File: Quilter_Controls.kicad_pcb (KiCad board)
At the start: 2 copper layers, 40.4 x 110 mm, 19 parts, among them J1 Conn_01x10_Male, J10 Conn_01x04_Male, J11 Freq_In, J2 Conn_01x10_Male, J3 Conn_01x10_Male, J4 Audio_In, J5 Audio_Out, J6 Audio_Mix, J7 Freq_V_Oct, J8 Freq_CV, J9 Conn_02x04_Top_Bottom

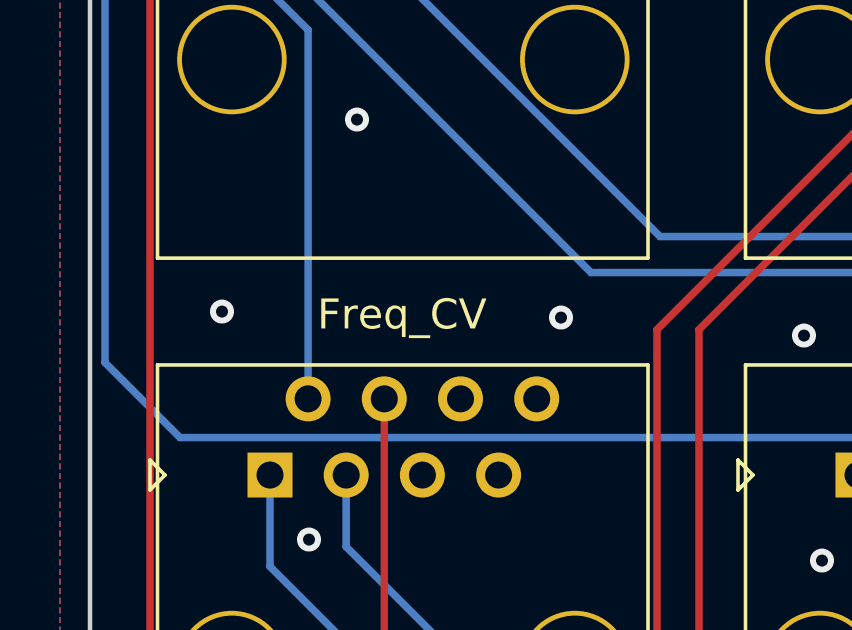
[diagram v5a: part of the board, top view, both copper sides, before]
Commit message: Cleaned up panel and PCBs
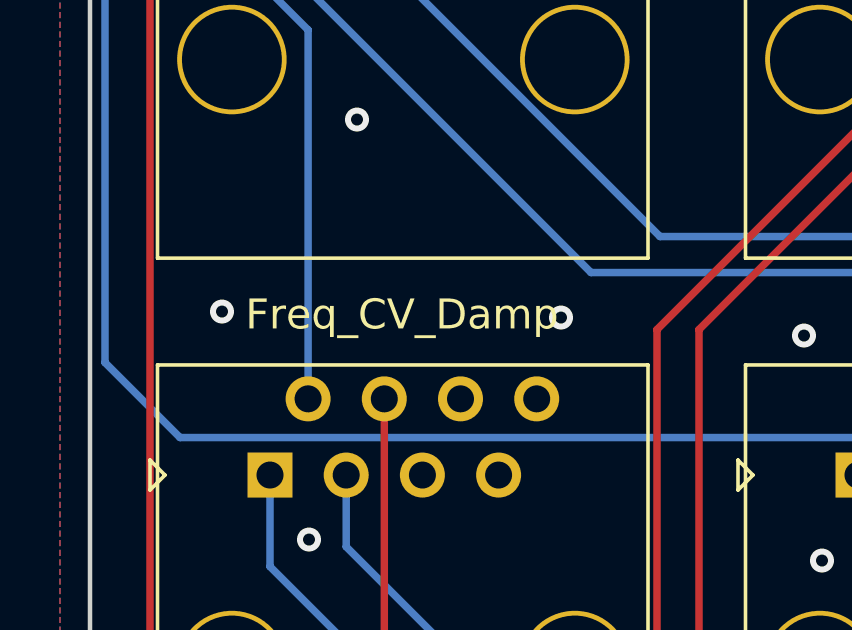
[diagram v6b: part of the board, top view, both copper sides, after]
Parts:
- J8: value Freq_CV -> Freq_CV_Damp
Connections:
- net /FREQ_CV1 renamed /FREQ_CV_DAMP1
- net /FREQ_CV2 renamed /FREQ_CV_DAMP2
- net /FREQ_CV3 renamed /FREQ_CV_DAMP3
- net /FREQ_CV4 renamed /FREQ_CV_DAMP4
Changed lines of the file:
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@@
       (outputformat 1)
       (mirror false)
-      (drillshape 1)
+      (drillshape 0)
       (scaleselection 1)
-      (outputdirectory "")
+      (outputdirectory "Gerbers/Controls/")
     )
   )
@@
   (net 11 "/FREQ_V_OCT2")
   (net 12 "/FREQ_JACK")
-  (net 13 "/FREQ_CV2")
+  (net 13 "/FREQ_CV_DAMP2")
   (net 14 "/AUDIO_IN2")
   (net 15 "/FREQ_V_OCT4")
-  (net 16 "/FREQ_CV4")
+  (net 16 "/FREQ_CV_DAMP4")
   (net 17 "/Q_POT")
   (net 18 "/AUDIO_IN4")
-  (net 19 "/FREQ_CV1")
-  (net 20 "/FREQ_CV3")
+  (net 19 "/FREQ_CV_DAMP1")
+  (net 20 "/FREQ_CV_DAMP3")
   (net 21 "/AUDIO_IN3")
   (net 22 "/FREQ_V_OCT3")
@@
     )
     (fp_circle (center 0 0) (end 1.414214 0) (layer "F.SilkS") (width 0.12) (fill none))
-    (model "${KIPRJMOD}/Graphics/Quilter_Panel.step"
+    (model "${KIPRJMOD}/Graphics/Quilter_Panel.step" hide
       (offset (xyz 0 0 10.5))
       (scale (xyz 1 1 1))
@@
       (effects (font (size 1 1) (thickness 0.15)))
     )
-    (fp_text value "Freq_CV" (at 0 -10) (layer "F.SilkS")
+    (fp_text value "Freq_CV_Damp" (at 0 -10) (layer "F.SilkS")
       (effects (font (size 1 1) (thickness 0.15)))
     )
@@
     (pad "" np_thru_hole circle (at -5.67 1.7) (size 3.65 3.65) (drill 3.33) (layers F&B.Cu *.SilkS *.Mask))
     (pad "1" thru_hole rect (at -4.4 -4.65) (size 1.5 1.5) (drill 0.9) (layers *.Cu *.Mask)
-      (net 19 "/FREQ_CV1") (pintype "passive"))
+      (net 19 "/FREQ_CV_DAMP1") (pintype "passive"))
     (pad "2" thru_hole circle (at -3.13 -7.19) (size 1.5 1.5) (drill 0.9) (layers *.Cu *.Mask)
-      (net 13 "/FREQ_CV2") (pintype "passive"))
+      (net 13 "/FREQ_CV_DAMP2") (pintype "passive"))
     (pad "3" thru_hole circle (at -1.86 -4.65) (size 1.5 1.5) (drill 0.9) (layers *.Cu *.Mask)
-      (net 20 "/FREQ_CV3") (pintype "passive"))
+      (net 20 "/FREQ_CV_DAMP3") (pintype "passive"))
     (pad "4" thru_hole circle (at -0.59 -7.19) (size 1.5 1.5) (drill 0.9) (layers *.Cu *.Mask)
-      (net 16 "/FREQ_CV4") (pintype "passive"))
+      (net 16 "/FREQ_CV_DAMP4") (pintype "passive"))
     (pad "5" thru_hole circle (at 0.68 -4.65) (size 1.5 1.5) (drill 0.9) (layers *.Cu *.Mask)
       (net 36 "unconnected-(J8-Pad5)") (pintype "passive+no_connect"))
@@
       (net 15 "/FREQ_V_OCT4") (pinfunction "Pin_2") (pintype "passive"))
     (pad "3" thru_hole oval locked (at 0 -5.08 270) (size 1.7 1.7) (drill 1) (layers F&B.Cu *.Mask)
-      (net 16 "/FREQ_CV4") (pinfunction "Pin_3") (pintype "passive"))
+      (net 16 "/FREQ_CV_DAMP4") (pinfunction "Pin_3") (pintype "passive"))
     (pad "4" thru_hole oval locked (at 0 -7.62 270) (size 1.7 1.7) (drill 1) (layers F&B.Cu *.Mask)
       (net 1 "GND") (pinfunction "Pin_4") (pintype "passive"))
@@
       (net 1 "GND") (pinfunction "Pin_6") (pintype "passive"))
     (pad "7" thru_hole oval locked (at 0 -15.24 270) (size 1.7 1.7) (drill 1) (layers F&B.Cu *.Mask)
-      (net 19 "/FREQ_CV1") (pinfunction "Pin_7") (pintype "passive"))
+      (net 19 "/FREQ_CV_DAMP1") (pinfunction "Pin_7") (pintype "passive"))
     (pad "8" thru_hole oval locked (at 0 -17.78 270) (size 1.7 1.7) (drill 1) (layers F&B.Cu *.Mask)
       (net 12 "/FREQ_JACK") (pinfunction "Pin_8") (pintype "passive"))
     (pad "9" thru_hole oval locked (at 0 -20.32 270) (size 1.7 1.7) (drill 1) (layers F&B.Cu *.Mask)
-      (net 20 "/FREQ_CV3") (pinfunction "Pin_9") (pintype "passive"))
+      (net 20 "/FREQ_CV_DAMP3") (pinfunction "Pin_9") (pintype "passive"))
     (pad "10" thru_hole oval locked (at 0 -22.86 270) (size 1.7 1.7) (drill 1) (layers F&B.Cu *.Mask)
       (net 22 "/FREQ_V_OCT3") (pinfunction "Pin_10") (pintype "passive"))
@@
       (net 8 "/AUDIO_IN1") (pinfunction "Pin_8") (pintype "passive"))
     (pad "9" thru_hole oval locked (at 0 -20.32 180) (size 1.7 1.7) (drill 1) (layers F&B.Cu *.Mask)
-      (net 13 "/FREQ_CV2") (pinfunction "Pin_9") (pintype "passive"))
+      (net 13 "/FREQ_CV_DAMP2") (pinfunction "Pin_9") (pintype "passive"))
     (pad "10" thru_hole oval locked (at 0 -22.86 180) (size 1.7 1.7) (drill 1) (layers F&B.Cu *.Mask)
       (net 11 "/FREQ_V_OCT2") (pinfunction "Pin_10") (pintype "passive"))
@@
     )
     (fp_circle (center 0 0) (end 1.414214 0) (layer "B.SilkS") (width 0.12) (fill none))
-    (model "${KIPRJMOD}/Graphics/Quilter_Components.step"
+    (model "${KIPRJMOD}/Graphics/Quilter_Components.step" hide
       (offset (xyz 0 0 10))
       (scale (xyz 1 1 1))

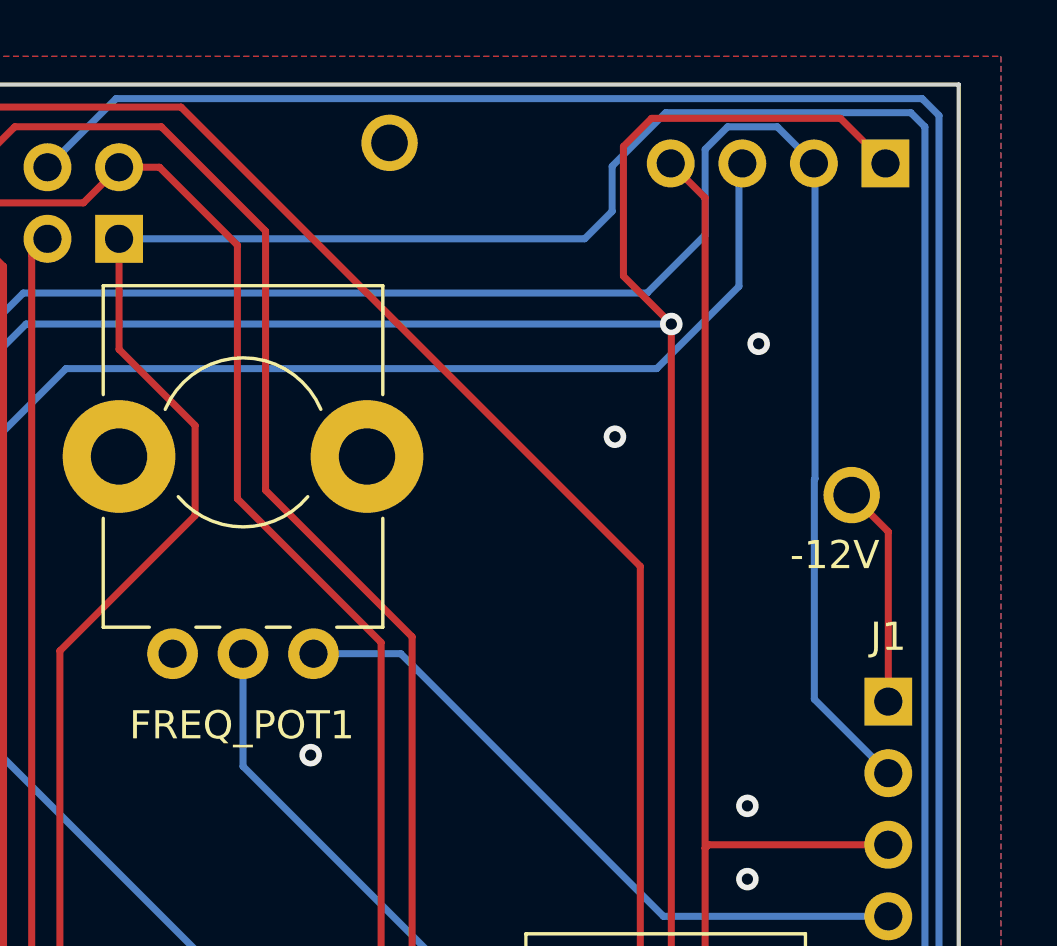
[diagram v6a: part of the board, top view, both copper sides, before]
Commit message: Updates for v2, including dc blocking caps on output
Also adjusted lower range of cutoff knob and tweaked various resistor values
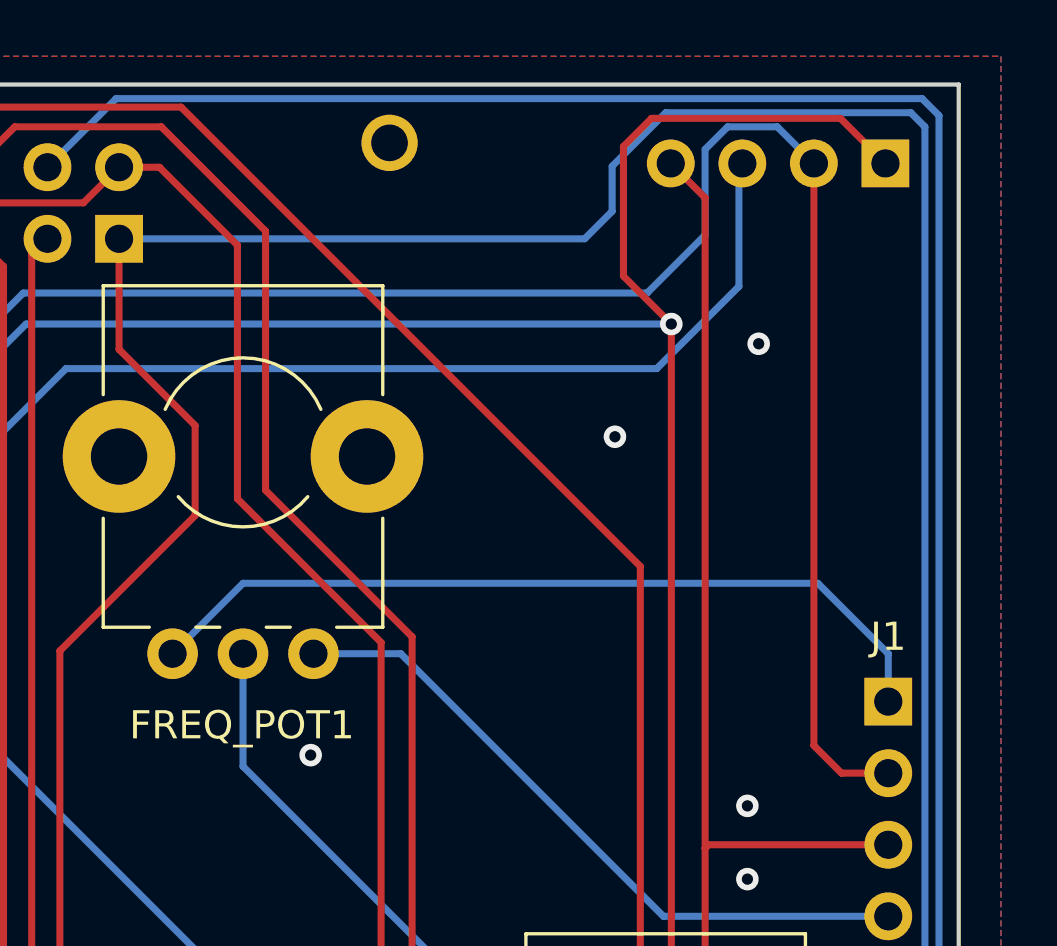
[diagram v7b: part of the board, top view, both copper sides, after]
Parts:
- removed TP2: TestPoint, Custom_Footprints:1.3mm_Test_Point
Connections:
- FREQ_POT1 pad 3: GND -> /FREQ_POT_-5V
- J1 pad 1: -12V -> /FREQ_POT_-5V
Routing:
- net /FREQ_POT_-5V: track 0.00 -> 29.2 mm
- net -12V: track 7.87 -> 0.00 mm
- net /AUDIO_BUFF2: track 153.7 -> 154.6 mm
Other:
- board text removed: "-12V"
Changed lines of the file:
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@@
   (net 39 "unconnected-(J8-Pad8)")
   (net 40 "+12V")
-  (net 41 "-12V")
+  (net 41 "/FREQ_POT_-5V")
   (footprint "Custom_Footprints:3D_Dummy" (layer "F.Cu")
     (at 70.2 95.7)
@@
     )
   )
-  (footprint "Custom_Footprints:1.3mm_Test_Point" (layer "F.Cu")
-    (at 86.6 55.47)
-    (descr "1.3mm Test Point")
-    (tags "Through Hole Mount Test Points")
-    (property "Sheetfile" "Quilter_Controls.kicad_sch")
-    (property "Sheetname" "")
-    (attr exclude_from_pos_files)
-    (fp_text reference "TP2" (at 0 -2.75) (layer "F.SilkS") hide
-      (effects (font (size 1 1) (thickness 0.15)))
-    )
-    (fp_text value "TestPoint" (at 0 2.75) (layer "F.Fab")
-      (effects (font (size 1 1) (thickness 0.15)))
-    )
-    (fp_circle (center 0 0) (end 1.05 0) (layer "F.CrtYd") (width 0.05) (fill none))
-    (fp_line (start -1.25 0.4) (end -1.25 -0.4) (layer "F.Fab") (width 0.15))
-    (fp_line (start 1.25 0.4) (end -1.25 0.4) (layer "F.Fab") (width 0.15))
-    (fp_line (start 1.25 -0.4) (end 1.25 0.4) (layer "F.Fab") (width 0.15))
-    (fp_line (start -1.25 -0.4) (end 1.25 -0.4) (layer "F.Fab") (width 0.15))
-    (pad "1" thru_hole circle locked (at 0 0) (size 2 2) (drill 1.3) (layers *.Cu *.Mask)
-      (net 41 "-12V") (pinfunction "1") (pintype "passive"))
-  )
   (footprint "Custom_Footprints:RJ45_Molex_42878-8506" (layer "F.Cu")
     (at 60.4 103.9)
@@
       (net 2 "/FREQ_POT") (pinfunction "2") (pintype "passive"))
     (pad "3" thru_hole circle locked (at -2.5 7.5 90) (size 1.8 1.8) (drill 1) (layers *.Cu *.Mask)
-      (net 1 "GND") (pinfunction "3") (pintype "passive"))
+      (net 41 "/FREQ_POT_-5V") (pinfunction "3") (pintype "passive"))
     (model "${CUSTOM_3D}/ALPHA-RD901F-40.step"
       (offset (xyz -0 -0.2 0))
@@
     (fp_line (start -1.27 -24.13) (end -1.27 0.635) (layer "B.Fab") (width 0.1))
     (pad "1" thru_hole rect locked (at 0 0 180) (size 1.7 1.7) (drill 1) (layers F&B.Cu *.Mask)
-      (net 41 "-12V") (pinfunction "Pin_1") (pintype "passive"))
+      (net 41 "/FREQ_POT_-5V") (pinfunction "Pin_1") (pintype "passive"))
     (pad "2" thru_hole oval locked (at 0 -2.54 180) (size 1.7 1.7) (drill 1) (layers F&B.Cu *.Mask)
       (net 10 "/AUDIO_BUFF2") (pinfunction "Pin_2") (pintype "passive"))
@@
   (gr_text "V/O" (at 64.5 46.4) (layer "B.SilkS")
     (effects (font (size 1.2 1.2) (thickness 0.2)) (justify mirror))
-  )
-  (gr_text "-12V" (at 86.8 57.5) (layer "B.SilkS")
-    (effects (font (size 1 1) (thickness 0.2)) (justify mirror))
-  )
-  (gr_text "-12V" (at 86 57.6) (layer "F.SilkS")
-    (effects (font (size 1 1) (thickness 0.2)))
   )
   (gr_text "J3" (at 56.4 147.9) (layer "F.SilkS")
@@
   (segment (start 78.14 119.45) (end 78.14 113.74) (width 0.25) (layer "B.Cu") (net 9))
   (segment (start 56.5 53.2) (end 56.5 56) (width 0.25) (layer "B.Cu") (net 9))
+  (segment (start 87.9 65.34) (end 86.24 65.34) (width 0.25) (layer "F.Cu") (net 10))
+  (segment (start 86.24 65.34) (end 85.26 64.36) (width 0.25) (layer "F.Cu") (net 10))
+  (segment (start 85.26 64.36) (end 85.26 43.7) (width 0.25) (layer "F.Cu") (net 10))
   (segment (start 50.5 55) (end 50.5 115.7) (width 0.25) (layer "B.Cu") (net 10))
   (segment (start 57.2 48.3) (end 50.5 55) (width 0.25) (layer "B.Cu") (net 10))
   (segment (start 83.96 42.4) (end 82.2 42.4) (width 0.25) (layer "B.Cu") (net 10))
-  (segment (start 85.3 43.74) (end 85.26 43.7) (width 0.25) (layer "B.Cu") (net 10))
   (segment (start 81.4 46.242081) (end 79.342081 48.3) (width 0.25) (layer "B.Cu") (net 10))
-  (segment (start 85.3 54.896167) (end 85.3 43.74) (width 0.25) (layer "B.Cu") (net 10))
   (segment (start 50.5 115.7) (end 53 118.2) (width 0.25) (layer "B.Cu") (net 10))
-  (segment (start 85.275 54.921167) (end 85.3 54.896167) (width 0.25) (layer "B.Cu") (net 10))
-  (segment (start 85.275 62.715) (end 85.275 54.921167) (width 0.25) (layer "B.Cu") (net 10))
   (segment (start 82.2 42.4) (end 81.4 43.2) (width 0.25) (layer "B.Cu") (net 10))
   (segment (start 79.342081 48.3) (end 57.2 48.3) (width 0.25) (layer "B.Cu") (net 10))
   (segment (start 53 118.2) (end 75.58 118.2) (width 0.25) (layer "B.Cu") (net 10))
   (segment (start 85.26 43.7) (end 83.96 42.4) (width 0.25) (layer "B.Cu") (net 10))
-  (segment (start 87.9 65.34) (end 85.275 62.715) (width 0.25) (layer "B.Cu") (net 10))
   (segment (start 75.58 118.2) (end 76.87 116.91) (width 0.25) (layer "B.Cu") (net 10))
   (segment (start 81.4 43.2) (end 81.4 46.242081) (width 0.25) (layer "B.Cu") (net 10))
@@
   (segment (start 54.4 62.7) (end 73.2 81.5) (width 0.25) (layer "B.Cu") (net 40))
   (segment (start 73.2 81.5) (end 79.9 81.5) (width 0.25) (layer "B.Cu") (net 40))
-  (segment (start 86.6 55.47) (end 87.9 56.77) (width 0.25) (layer "F.Cu") (net 41))
-  (segment (start 87.9 56.77) (end 87.9 62.8) (width 0.25) (layer "F.Cu") (net 41))
+  (segment (start 87.9 61.1) (end 85.4 58.6) (width 0.25) (layer "B.Cu") (net 41))
+  (segment (start 85.4 58.6) (end 65 58.6) (width 0.25) (layer "B.Cu") (net 41))
+  (segment (start 65 58.6) (end 62.5 61.1) (width 0.25) (layer "B.Cu") (net 41))
+  (segment (start 87.9 62.8) (end 87.9 61.1) (width 0.25) (layer "B.Cu") (net 41))
   (zone (net 1) (net_name "GND") (layers F&B.Cu) (hatch edge 0.508)
     (connect_pads (clearance 0.508))
